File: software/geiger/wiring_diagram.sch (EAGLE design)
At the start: 7 parts

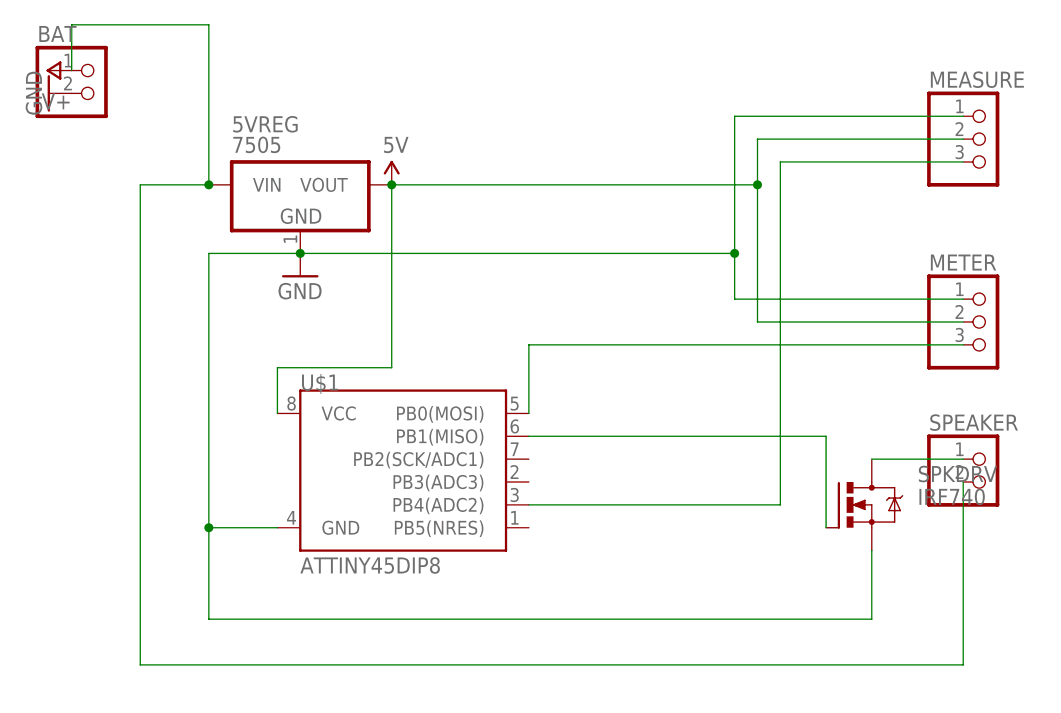
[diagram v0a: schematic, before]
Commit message: added the speaker supply cap and made more clear that the speaker ground should be connected near battery ground
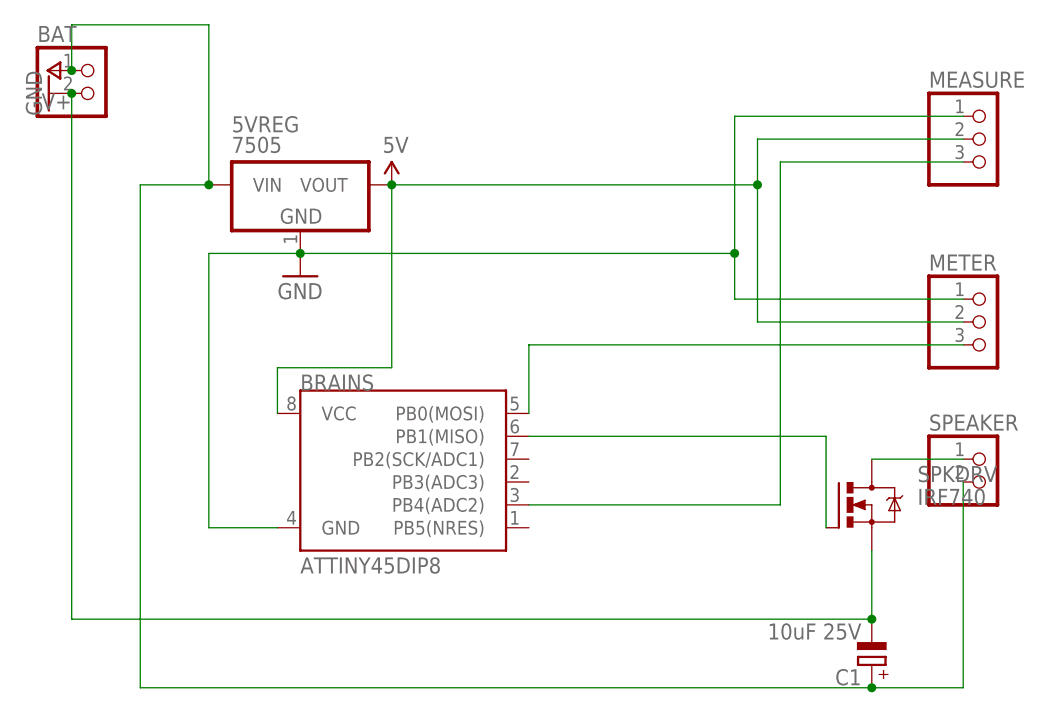
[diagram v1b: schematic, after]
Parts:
- added C1: 10uF 25V, rcl:CPOL-EUE2-4
- renumbered U$1 to BRAINS
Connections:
- net GND: now also C1.-
- net V+: now also C1.+
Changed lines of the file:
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@@
 </classes>
 <parts>
-<part name="U$1" library="SparkFun-DigitalIC" deviceset="ATTINY45" device="DIP8"/>
+<part name="BRAINS" library="SparkFun-DigitalIC" deviceset="ATTINY45" device="DIP8"/>
 <part name="5VREG" library="dp_devices" deviceset="IC_VREG_3PINS" device="-TO-220" value="7505"/>
 <part name="MEASURE" library="pinhead" deviceset="PINHD-1X3" device=""/>
@@
 <part name="P+1" library="supply1" deviceset="V+" device=""/>
 <part name="SPKDRV" library="transistor-power" deviceset="IRF740" device=""/>
+<part name="C1" library="rcl" deviceset="CPOL-EU" device="E2-4" value="10uF 25V"/>
 </parts>
 <sheets>
@@
 </plain>
 <instances>
-<instance part="U$1" gate="G$1" x="50.8" y="50.8"/>
+<instance part="BRAINS" gate="G$1" x="50.8" y="50.8"/>
 <instance part="5VREG" gate="VREG" x="38.1" y="83.82"/>
 <instance part="MEASURE" gate="A" x="114.3" y="88.9"/>
@@
 <instance part="P+1" gate="1" x="10.16" y="96.52" rot="R90"/>
 <instance part="SPKDRV" gate="G$1" x="99.06" y="48.26"/>
+<instance part="C1" gate="G$1" x="101.6" y="30.48" rot="R180"/>
 </instances>
 <busses>
@@
 <wire x1="86.36" y1="71.12" x2="86.36" y2="76.2" width="0.1524" layer="91"/>
 <junction x="86.36" y="76.2"/>
-<pinref part="U$1" gate="G$1" pin="GND"/>
+<pinref part="BRAINS" gate="G$1" pin="GND"/>
 <wire x1="35.56" y1="45.72" x2="27.94" y2="45.72" width="0.1524" layer="91"/>
 <wire x1="27.94" y1="45.72" x2="27.94" y2="76.2" width="0.1524" layer="91"/>
-<pinref part="SPKDRV" gate="G$1" pin="S"/>
-<wire x1="101.6" y1="43.18" x2="101.6" y2="35.56" width="0.1524" layer="91"/>
-<wire x1="101.6" y1="35.56" x2="27.94" y2="35.56" width="0.1524" layer="91"/>
-<wire x1="27.94" y1="35.56" x2="27.94" y2="45.72" width="0.1524" layer="91"/>
-<junction x="27.94" y="45.72"/>
 </segment>
 <segment>
 <pinref part="BAT" gate="G$1" pin="2"/>
 <pinref part="GND2" gate="1" pin="GND"/>
+<pinref part="SPKDRV" gate="G$1" pin="S"/>
+<wire x1="101.6" y1="43.18" x2="101.6" y2="35.56" width="0.1524" layer="91"/>
+<pinref part="C1" gate="G$1" pin="-"/>
+<junction x="101.6" y="35.56"/>
+<wire x1="101.6" y1="35.56" x2="12.7" y2="35.56" width="0.1524" layer="91"/>
+<wire x1="12.7" y1="35.56" x2="12.7" y2="93.98" width="0.1524" layer="91"/>
+<junction x="12.7" y="93.98"/>
 </segment>
 </net>
@@
 <pinref part="U$2" gate="G$1" pin="5V"/>
 <wire x1="48.26" y1="83.82" x2="48.26" y2="63.5" width="0.1524" layer="91"/>
-<pinref part="U$1" gate="G$1" pin="VCC"/>
+<pinref part="BRAINS" gate="G$1" pin="VCC"/>
 <wire x1="48.26" y1="63.5" x2="35.56" y2="63.5" width="0.1524" layer="91"/>
 <wire x1="35.56" y1="63.5" x2="35.56" y2="58.42" width="0.1524" layer="91"/>
@@
 <wire x1="27.94" y1="101.6" x2="27.94" y2="83.82" width="0.1524" layer="91"/>
 <pinref part="SPEAKER" gate="G$1" pin="2"/>
-<wire x1="111.76" y1="50.8" x2="111.76" y2="30.48" width="0.1524" layer="91"/>
-<wire x1="111.76" y1="30.48" x2="20.32" y2="30.48" width="0.1524" layer="91"/>
-<wire x1="20.32" y1="30.48" x2="20.32" y2="83.82" width="0.1524" layer="91"/>
+<wire x1="111.76" y1="50.8" x2="111.76" y2="27.94" width="0.1524" layer="91"/>
+<wire x1="111.76" y1="27.94" x2="101.6" y2="27.94" width="0.1524" layer="91"/>
+<wire x1="101.6" y1="27.94" x2="20.32" y2="27.94" width="0.1524" layer="91"/>
+<wire x1="20.32" y1="27.94" x2="20.32" y2="83.82" width="0.1524" layer="91"/>
 <wire x1="20.32" y1="83.82" x2="27.94" y2="83.82" width="0.1524" layer="91"/>
 <junction x="27.94" y="83.82"/>
+<pinref part="C1" gate="G$1" pin="+"/>
+<junction x="101.6" y="27.94"/>
+<junction x="12.7" y="96.52"/>
 </segment>
 </net>
 <net name="N$1" class="0">
 <segment>
-<pinref part="U$1" gate="G$1" pin="PB4(ADC2)"/>
+<pinref part="BRAINS" gate="G$1" pin="PB4(ADC2)"/>
 <wire x1="63.5" y1="48.26" x2="91.44" y2="48.26" width="0.1524" layer="91"/>
 <wire x1="91.44" y1="48.26" x2="91.44" y2="86.36" width="0.1524" layer="91"/>
@@
 <segment>
 <pinref part="METER" gate="A" pin="3"/>
-<pinref part="U$1" gate="G$1" pin="PB0(MOSI)"/>
+<pinref part="BRAINS" gate="G$1" pin="PB0(MOSI)"/>
 <wire x1="111.76" y1="66.04" x2="63.5" y2="66.04" width="0.1524" layer="91"/>
 <wire x1="63.5" y1="66.04" x2="63.5" y2="58.42" width="0.1524" layer="91"/>
@@
 <net name="N$5" class="0">
 <segment>
-<pinref part="U$1" gate="G$1" pin="PB1(MISO)"/>
+<pinref part="BRAINS" gate="G$1" pin="PB1(MISO)"/>
 <pinref part="SPKDRV" gate="G$1" pin="G"/>
 <wire x1="63.5" y1="55.88" x2="96.52" y2="55.88" width="0.1524" layer="91"/>

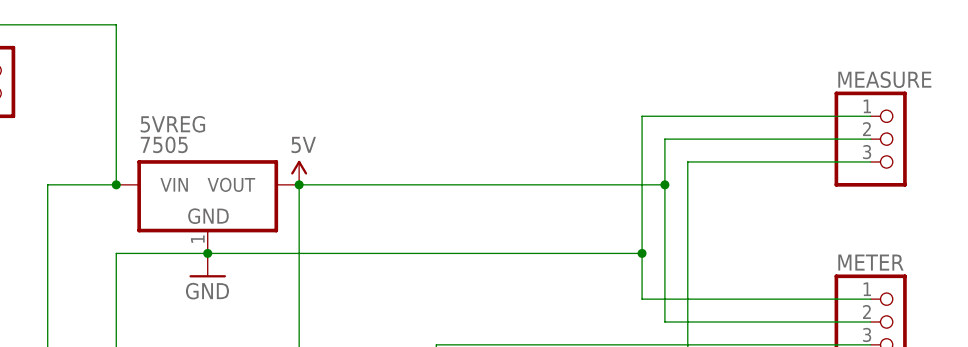
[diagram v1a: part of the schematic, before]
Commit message: note about optional cap on 7505 output
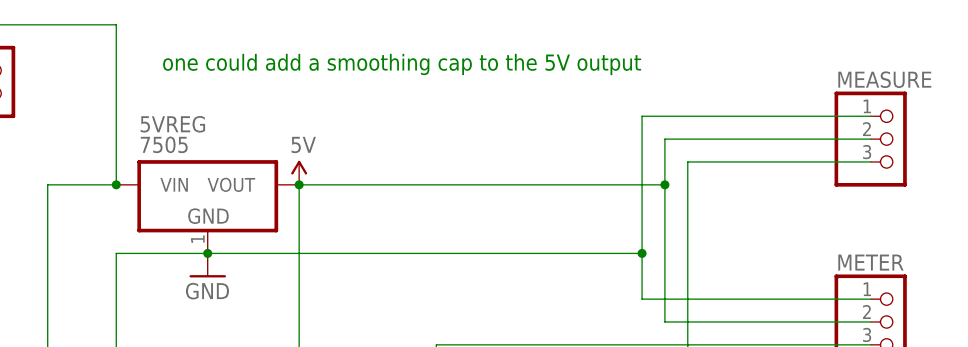
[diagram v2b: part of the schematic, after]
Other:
- note added: "one could add a smoothing cap to the 5V output"
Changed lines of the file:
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@@
 <sheet>
 <plain>
+<text x="33.02" y="96.52" size="1.778" layer="91">one could add a smoothing cap to the 5V output</text>
 </plain>
 <instances>
